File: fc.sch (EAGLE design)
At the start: 72 parts, among them IC1 BN055, J1 USBC, U1 LMZ21700, U2 ATMEGA2560-16AU100A-M, U3 SI8621AB-B-IS, U4 FT230XQ, Y1 16MHz, Y2 32.768kHz

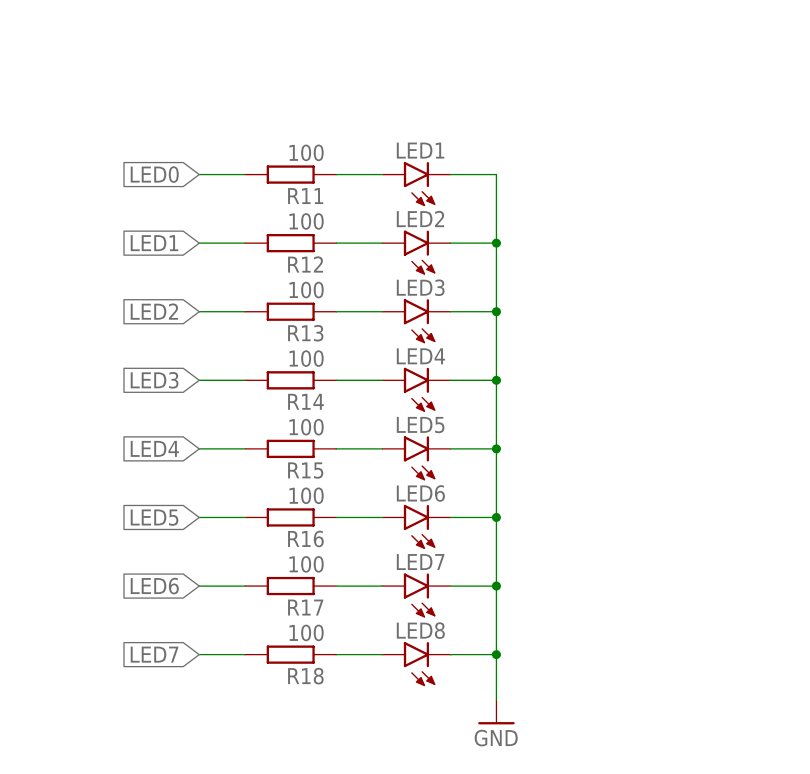
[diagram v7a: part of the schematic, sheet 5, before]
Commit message: changed LEDs to sparkfun lib
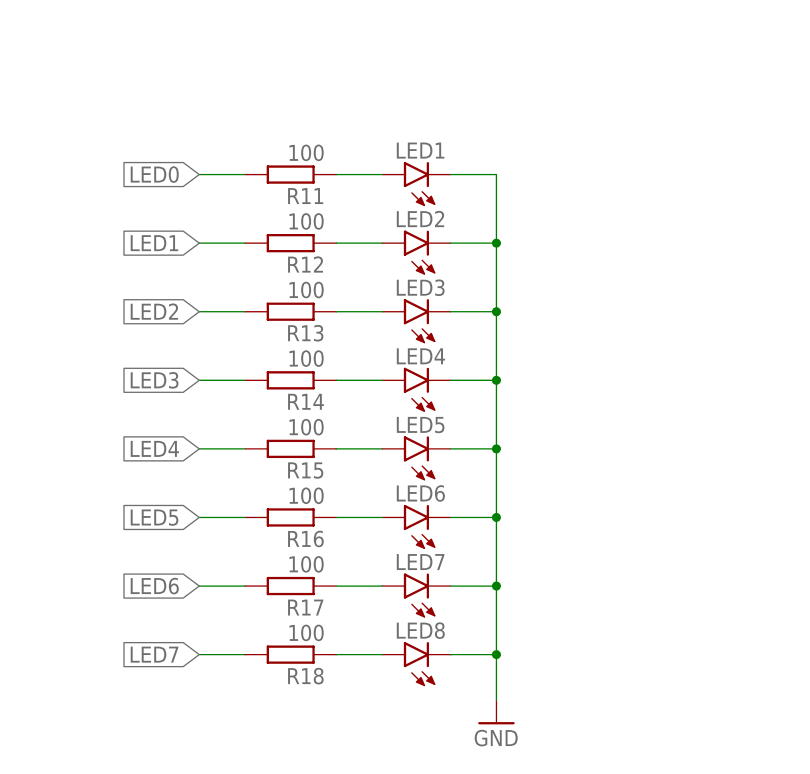
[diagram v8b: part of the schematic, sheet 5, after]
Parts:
- LED1, LED2, LED3, LED4, LED5, LED6, LED7, LED8: device led:LEDCHIP-LED0603 -> SparkFun-LED:LED0603
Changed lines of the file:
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@@
 <part name="GND16" library="supply1" library_urn="urn:adsk.eagle:library:371" deviceset="GND" device=""/>
 <part name="R11" library="rcl" library_urn="urn:adsk.eagle:library:334" deviceset="R-EU_" device="R0603" package3d_urn="urn:adsk.eagle:package:23555/2" value="100"/>
-<part name="LED1" library="led" library_urn="urn:adsk.eagle:library:259" deviceset="LED" device="CHIP-LED0603" package3d_urn="urn:adsk.eagle:package:15819/3"/>
+<part name="LED1" library="SparkFun-LED" library_urn="urn:adsk.eagle:library:529" deviceset="LED" device="0603" package3d_urn="urn:adsk.eagle:package:39354/1"/>
 <part name="GND17" library="supply1" library_urn="urn:adsk.eagle:library:371" deviceset="GND" device=""/>
 <part name="R12" library="rcl" library_urn="urn:adsk.eagle:library:334" deviceset="R-EU_" device="R0603" package3d_urn="urn:adsk.eagle:package:23555/2" value="100"/>
-<part name="LED2" library="led" library_urn="urn:adsk.eagle:library:259" deviceset="LED" device="CHIP-LED0603" package3d_urn="urn:adsk.eagle:package:15819/3"/>
+<part name="LED2" library="SparkFun-LED" library_urn="urn:adsk.eagle:library:529" deviceset="LED" device="0603" package3d_urn="urn:adsk.eagle:package:39354/1"/>
 <part name="R13" library="rcl" library_urn="urn:adsk.eagle:library:334" deviceset="R-EU_" device="R0603" package3d_urn="urn:adsk.eagle:package:23555/2" value="100"/>
-<part name="LED3" library="led" library_urn="urn:adsk.eagle:library:259" deviceset="LED" device="CHIP-LED0603" package3d_urn="urn:adsk.eagle:package:15819/3"/>
+<part name="LED3" library="SparkFun-LED" library_urn="urn:adsk.eagle:library:529" deviceset="LED" device="0603" package3d_urn="urn:adsk.eagle:package:39354/1"/>
 <part name="R14" library="rcl" library_urn="urn:adsk.eagle:library:334" deviceset="R-EU_" device="R0603" package3d_urn="urn:adsk.eagle:package:23555/2" value="100"/>
-<part name="LED4" library="led" library_urn="urn:adsk.eagle:library:259" deviceset="LED" device="CHIP-LED0603" package3d_urn="urn:adsk.eagle:package:15819/3"/>
+<part name="LED4" library="SparkFun-LED" library_urn="urn:adsk.eagle:library:529" deviceset="LED" device="0603" package3d_urn="urn:adsk.eagle:package:39354/1"/>
 <part name="R15" library="rcl" library_urn="urn:adsk.eagle:library:334" deviceset="R-EU_" device="R0603" package3d_urn="urn:adsk.eagle:package:23555/2" value="100"/>
-<part name="LED5" library="led" library_urn="urn:adsk.eagle:library:259" deviceset="LED" device="CHIP-LED0603" package3d_urn="urn:adsk.eagle:package:15819/3"/>
+<part name="LED5" library="SparkFun-LED" library_urn="urn:adsk.eagle:library:529" deviceset="LED" device="0603" package3d_urn="urn:adsk.eagle:package:39354/1"/>
 <part name="R16" library="rcl" library_urn="urn:adsk.eagle:library:334" deviceset="R-EU_" device="R0603" package3d_urn="urn:adsk.eagle:package:23555/2" value="100"/>
-<part name="LED6" library="led" library_urn="urn:adsk.eagle:library:259" deviceset="LED" device="CHIP-LED0603" package3d_urn="urn:adsk.eagle:package:15819/3"/>
+<part name="LED6" library="SparkFun-LED" library_urn="urn:adsk.eagle:library:529" deviceset="LED" device="0603" package3d_urn="urn:adsk.eagle:package:39354/1"/>
 <part name="R17" library="rcl" library_urn="urn:adsk.eagle:library:334" deviceset="R-EU_" device="R0603" package3d_urn="urn:adsk.eagle:package:23555/2" value="100"/>
-<part name="LED7" library="led" library_urn="urn:adsk.eagle:library:259" deviceset="LED" device="CHIP-LED0603" package3d_urn="urn:adsk.eagle:package:15819/3"/>
+<part name="LED7" library="SparkFun-LED" library_urn="urn:adsk.eagle:library:529" deviceset="LED" device="0603" package3d_urn="urn:adsk.eagle:package:39354/1"/>
 <part name="R18" library="rcl" library_urn="urn:adsk.eagle:library:334" deviceset="R-EU_" device="R0603" package3d_urn="urn:adsk.eagle:package:23555/2" value="100"/>
-<part name="LED8" library="led" library_urn="urn:adsk.eagle:library:259" deviceset="LED" device="CHIP-LED0603" package3d_urn="urn:adsk.eagle:package:15819/3"/>
+<part name="LED8" library="SparkFun-LED" library_urn="urn:adsk.eagle:library:529" deviceset="LED" device="0603" package3d_urn="urn:adsk.eagle:package:39354/1"/>
 <part name="JP1" library="pinhead" library_urn="urn:adsk.eagle:library:325" deviceset="PINHD-1X3" device="" package3d_urn="urn:adsk.eagle:package:22458/2"/>
 <part name="P+8" library="supply1" library_urn="urn:adsk.eagle:library:371" deviceset="+5V" device=""/>
